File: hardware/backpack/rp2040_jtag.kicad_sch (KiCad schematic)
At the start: 27 parts, among them U1 ZD25WQ16CSIGT(SOIC-8_208mils), U2 RP2040(QFN-56_7x7mm_P0.4mm), Y1 Crystal_GND24_Small

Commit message: start power
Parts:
- removed RP-BOOT1: YTS-A016-X, symbol OLIMEX_Buttons:T1107A(6x3,8x2,5MM)
- added SW2: ~, cynthion:SW_Tactile_SPST_Angled_TC-1109DE-B-F, symbol support_hardware:SW_SPST_shielded
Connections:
- net GND: now also SW2.1
- net ~{BOOTSEL}: now also SW2.2
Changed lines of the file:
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@@
-	)
-	(symbol
-		(lib_id "OLIMEX_Buttons:T1107A(6x3,8x2,5MM)")
-		(at 186.69 33.02 0)
-		(unit 1)
-		(exclude_from_sim no)
-		(in_bom yes)
-		(on_board yes)
-		(dnp no)
-		(property "Reference" "RP-BOOT1"
-			(at 194.818 28.448 0)
-			(effects
-				(font
-					(size 1.524 1.524)
-				)
-			)
-		)
-		(property "Value" "YTS-A016-X"
-			(at 186.69 35.56 0)
-			(effects
-				(font
-					(size 1.27 1.27)
-				)
-			)
-		)
-		(property "Footprint" ""
-			(at 186.6646 32.0548 0)
-			(effects
-				(font
-					(size 1.524 1.524)
-				)
-				(hide yes)
-			)
-		)
-		(property "Datasheet" ""
-			(at 186.6646 32.0548 0)
-			(effects
-				(font
-					(size 1.524 1.524)
-				)
-			)
-		)
-		(property "Description" ""
-			(at 186.69 33.02 0)
-			(effects
-				(font
-					(size 1.27 1.27)
-				)
-				(hide yes)
-			)
-		)
-		(property "lcsc#" "C2910673"
-			(at 186.69 33.02 0)
-			(effects
-				(font
-					(size 1.27 1.27)
-				)
-				(hide yes)
-			)
-		)
-		(pin "1"
-		)
-		(pin "2"
-		)
-		(instances
-			(project "backpack"
-				(path "/df6062c3-a570-4505-924c-c7fe32df3670/32fbecb8-cfc0-4e90-9d95-f47a131c8376"
-					(reference "RP-BOOT1")
-					(unit 1)
-				)
-			)
-		)
 	)
 	(symbol
@@
 					(unit 1)
 				)
+			)
+		)
+	)
+	(symbol
+		(lib_id "support_hardware:SW_SPST_shielded")
+		(at 186.69 33.02 180)
+		(unit 1)
+		(exclude_from_sim no)
+		(in_bom yes)
+		(on_board yes)
+		(dnp no)
+		(property "Reference" "SW2"
+			(at 186.69 25.908 0)
+			(effects
+				(font
+					(size 1.27 1.27)
+				)
+			)
+		)
+		(property "Value" "~"
+			(at 186.69 25.4 0)
+			(effects
+				(font
+					(size 1.27 1.27)
+				)
+			)
+		)
+		(property "Footprint" "cynthion:SW_Tactile_SPST_Angled_TC-1109DE-B-F"
+			(at 186.69 33.02 0)
+			(effects
+				(font
+					(size 1.27 1.27)
+				)
+				(hide yes)
+			)
+		)
+		(property "Datasheet" "~"
+			(at 186.69 33.02 0)
+			(effects
+				(font
+					(size 1.27 1.27)
+				)
+				(hide yes)
+			)
+		)
+		(property "Description" "SWITCH TACTILE SPST-NO 0.05A 12V"
+			(at 186.69 33.02 0)
+			(effects
+				(font
+					(size 1.27 1.27)
+				)
+				(hide yes)
+			)
+		)
+		(property "Manufacturer" "XKB"
+			(at 186.69 33.02 0)
+			(effects
+				(font
+					(size 1.27 1.27)
+				)
+				(hide yes)
+			)
+		)
+		(property "Part Number" "TC-1109DE-B-F"
+			(at 186.69 33.02 0)
+			(effects
+				(font
+					(size 1.27 1.27)
+				)
+				(hide yes)
+			)
+		)
+		(property "Substitution" "DEALON TC-1150DL-6.0H-160"
+			(at 186.69 33.02 0)
+			(effects
+				(font
+					(size 1.27 1.27)
+				)
+				(hide yes)
+			)
+		)
+		(property "lcsc#" "C692468"
+			(at 186.69 33.02 0)
+			(effects
+				(font
+					(size 1.27 1.27)
+				)
+				(hide yes)
+			)
+		)
+		(pin "1"
+		)
+		(pin "2"
+		)
+		(pin "3"
+		)
+		(instances
+			(project "backpack"
+				(path "/df6062c3-a570-4505-924c-c7fe32df3670/32fbecb8-cfc0-4e90-9d95-f47a131c8376"
+					(reference "SW2")
+					(unit 1)
+				)

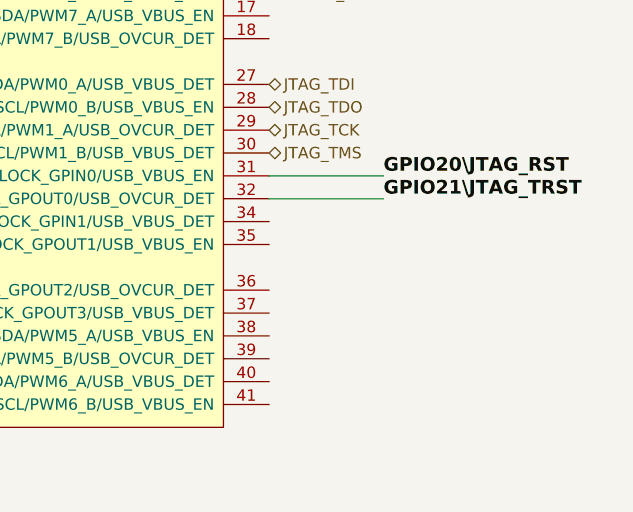
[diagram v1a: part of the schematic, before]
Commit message: parts and capture done sans most needing future pinswaps
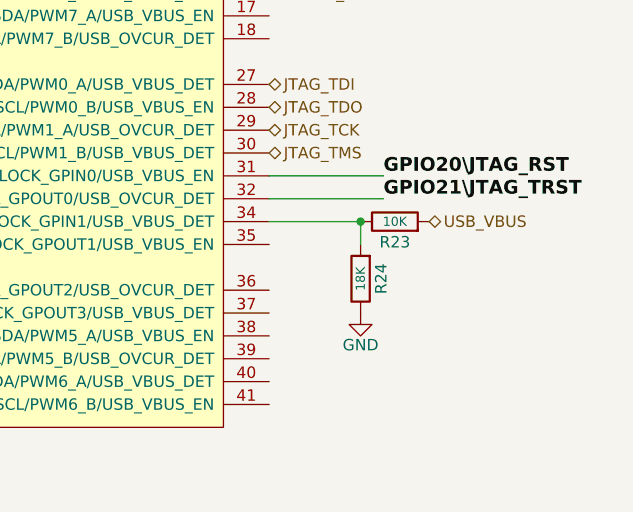
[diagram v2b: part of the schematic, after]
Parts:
- added R23: 10K, Resistor_SMD:R_0402_1005Metric, symbol OLIMEX_RCL:R
- added R24: 18K, Resistor_SMD:R_0402_1005Metric, symbol OLIMEX_RCL:R
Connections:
- net GND: now also R24.1
- net at U2.34 (GPIO22/SPI0_SCK/UART1_CTS/I2C1_SDA/PWM3_A/CLOCK_GPIN1/USB_VBUS_DET): now also R23.1, R24.2
- new net USB_VBUS: R23.2

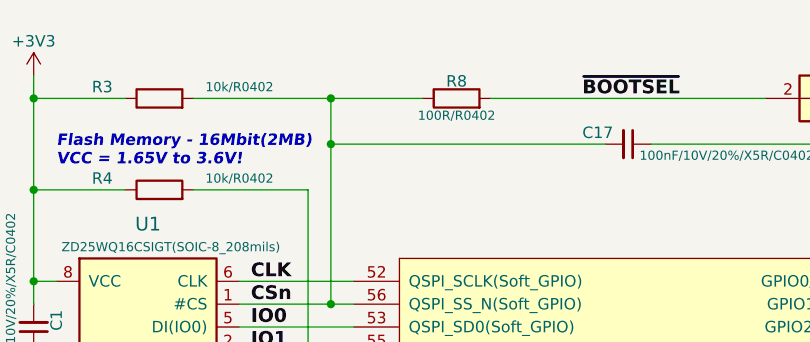
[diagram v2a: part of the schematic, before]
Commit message: place 2 leds, route 2nd button to both FPGA and RP2040
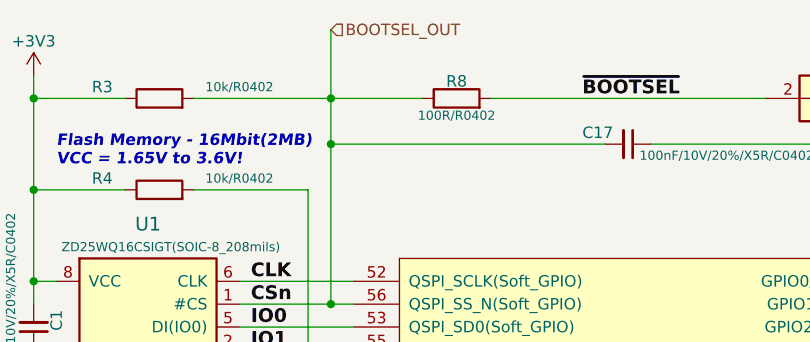
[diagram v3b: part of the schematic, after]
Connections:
- net CSn renamed BOOTSEL_OUT
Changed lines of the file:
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@@
+	(wire
+		(pts
+			(xy 130.81 25.4) (xy 130.81 33.02)
+		)
+		(stroke
+			(width 0)
+			(type default)
+		)
+	)
 	(wire
 		(pts
@@
 		)
 	)
+	(hierarchical_label "BOOTSEL_OUT"
+		(shape input)
+		(at 130.81 25.4 0)
+		(fields_autoplaced yes)
+		(effects
+			(font
+				(size 1.27 1.27)
+			)
+			(justify left)
+		)
+	)

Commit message: fix footprint errors and pin assignments on ffc
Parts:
- C11, C12: lcsc# (none) -> C12530
- C15, C16: lcsc# (none) -> C1549
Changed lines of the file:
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@@
+			)
+		)
+		(property "lcsc#" "C1549"
+			(at 102.87 132.08 0)
+			(effects
+				(font
+					(size 1.27 1.27)
+				)
+				(hide yes)
 			)
 		)
@@
 			)
 		)
+		(property "lcsc#" "C12530 "
+			(at 102.87 109.22 0)
+			(effects
+				(font
+					(size 1.27 1.27)
+				)
+				(hide yes)
+			)
+		)
 		(pin "1"
 		)
@@
 			)
 		)
+		(property "lcsc#" "C1549"
+			(at 102.87 137.16 0)
+			(effects
+				(font
+					(size 1.27 1.27)
+				)
+				(hide yes)
+			)
+		)
 		(pin "1"
 		)
@@
 			(at 102.87 114.3 0)
 			(effects
+				(font
+					(size 1.27 1.27)
+				)
+				(hide yes)
+			)
+		)
+		(property "lcsc#" "C12530 "
+			(at 102.87 114.3 0)
+			(effects

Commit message: updates before fab 04-04-24
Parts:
- C1, C10, C13, C14, C17, C2, C3, C4, C5, C6, C7, C8, C9: value 100nF/10V/20%/X5R/C0402 -> 0.1uF; lcsc# C129131 -> C307331
- R23: lcsc# C60490 -> C25744
- R24: lcsc# C60490 -> C138044
- R3, R4: value 10k/R0402 -> 10K; lcsc# C60490 -> C25744
- R5, R8: value 100R/R0402 -> 100R; lcsc# C106232 -> C25076
- R6, R7: value 27R/R0402 -> 27R
- SW2: value ~ -> SW_Tactile_SPST
- U1: footprint Package_SO:SOP-8_3.9x4.9mm_P1.27mm -> Package_SO:SOIC-8W_5.3x5.3mm_P1.27mm
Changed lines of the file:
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@@
 			)
 		)
-		(property "Value" "27R/R0402"
+		(property "Value" "27R"
 			(at 121.92 85.598 0)
 			(effects
@@
 			)
 		)
-		(property "Datasheet" ""
+		(property "Datasheet" "~"
 			(at 121.92 83.82 90)
 			(effects
@@
 			)
 		)
-		(property "Value" "100nF/10V/20%/X5R/C0402"
+		(property "Value" "0.1uF"
 			(at 104.14 87.63 90)
 			(effects
@@
 			)
 		)
-		(property "lcsc#" "C129131"
+		(property "lcsc#" " C307331"
 			(at 102.87 88.9 0)
 			(effects
@@
 			)
 		)
-		(property "Datasheet" ""
+		(property "Datasheet" "~"
 			(at 250.19 120.65 90)
 			(effects
@@
 			)
 		)
-		(property "lcsc#" "C60490"
+		(property "lcsc#" " C138044"
 			(at 250.19 120.65 0)
 			(effects
@@
 			)
 		)
-		(property "Value" "~"
+		(property "Value" "SW_Tactile_SPST"
 			(at 186.69 25.4 0)
 			(effects
@@
 			)
 		)
-		(property "lcsc#" "C60490"
+		(property "lcsc#" "C25744"
 			(at 254 114.3 0)
 			(effects
@@
 			)
 		)
-		(property "Value" "100nF/10V/20%/X5R/C0402"
+		(property "Value" "0.1uF"
 			(at 104.14 105.41 90)
 			(effects
@@
 			)
 		)
-		(property "lcsc#" "C129131"
+		(property "lcsc#" " C307331"
 			(at 102.87 106.68 0)
 			(effects
@@
 			)
 		)
-		(property "Value" "100R/R0402"
+		(property "Value" "100R"
 			(at 128.905 128.27 0)
 			(effects
@@
 			)
 		)
-		(property "Datasheet" ""
+		(property "Datasheet" "~"
 			(at 119.38 129.54 90)
 			(effects
@@
 			)
 		)
-		(property "lcsc#" "  C106232"
+		(property "lcsc#" "C25076"
 			(at 119.38 129.54 0)
 			(effects
@@
 			)
 		)
-		(property "Value" "100nF/10V/20%/X5R/C0402"
+		(property "Value" "0.1uF"
 			(at 104.14 100.33 90)
 			(effects
@@
 			)
 		)
-		(property "lcsc#" "C129131"
+		(property "lcsc#" " C307331"
 			(at 102.87 101.6 0)
 			(effects
@@
 			)
 		)
-		(property "Value" "100nF/10V/20%/X5R/C0402"
+		(property "Value" "0.1uF"
 			(at 104.14 120.65 90)
 			(effects
@@
 			)
 		)
-		(property "lcsc#" "C129131"
+		(property "lcsc#" " C307331"
 			(at 102.87 119.38 0)
 			(effects
@@
 			)
 		)
-		(property "Value" "100R/R0402"
+		(property "Value" "100R"
 			(at 144.78 34.925 0)
 			(effects
@@
 			)
 		)
-		(property "Datasheet" ""
+		(property "Datasheet" "~"
 			(at 144.78 33.02 90)
 			(effects
@@
 			)
 		)
-		(property "lcsc#" "  C106232"
+		(property "lcsc#" "C25076"
 			(at 144.78 33.02 0)
 			(effects
@@
 			)
 		)
-		(property "Datasheet" ""
+		(property "Datasheet" "~"
 			(at 102.87 132.08 0)
 			(effects
@@
 			)
 		)
-		(property "Value" "10k/R0402"
+		(property "Value" "10K"
 			(at 120.65 31.75 0)
 			(effects
@@
 			)
 		)
-		(property "lcsc#" "C60490"
+		(property "lcsc#" "C25744"
 			(at 111.76 33.02 0)
 			(effects
@@
 			)
 		)
-		(property "Footprint" "Package_SO:SOP-8_3.9x4.9mm_P1.27mm"
+		(property "Footprint" "Package_SO:SOIC-8W_5.3x5.3mm_P1.27mm"
 			(at 113.03 77.47 0)
 			(effects
@@
 			)
 		)
-		(property "Value" "100nF/10V/20%/X5R/C0402"
+		(property "Value" "0.1uF"
 			(at 104.14 97.79 90)
 			(effects
@@
 			)
 		)
-		(property "lcsc#" "C129131"
+		(property "lcsc#" " C307331"
 			(at 102.87 99.06 0)
 			(effects
@@
 			)
 		)
-		(property "Datasheet" ""
+		(property "Datasheet" "~"
 			(at 102.87 109.22 0)
 			(effects
@@
 			)
 		)
-		(property "Value" "27R/R0402"
+		(property "Value" "27R"
 			(at 121.92 79.375 0)
 			(effects
@@
 			)
 		)
-		(property "Datasheet" ""
+		(property "Datasheet" "~"
 			(at 121.92 81.28 90)
 			(effects
@@
 			)
 		)
-		(property "Value" "100nF/10V/20%/X5R/C0402"
+		(property "Value" "0.1uF"
 			(at 165.1 39.37 90)
 			(effects
@@
 			)
 		)
-		(property "lcsc#" "C129131"
+		(property "lcsc#" " C307331"
 			(at 163.83 38.1 0)
 			(effects
@@
 			)
 		)
-		(property "Value" "100nF/10V/20%/X5R/C0402"
+		(property "Value" "0.1uF"
 			(at 95.25 45.72 90)
 			(effects
@@
 			)
 		)
-		(property "lcsc#" "C129131"
+		(property "lcsc#" " C307331"
 			(at 97.79 58.42 0)
 			(effects
@@
 			)
 		)
-		(property "Value" "100nF/10V/20%/X5R/C0402"
+		(property "Value" "0.1uF"
 			(at 104.14 118.11 90)
 			(effects
@@
 			)
 		)
-		(property "lcsc#" "C129131"
+		(property "lcsc#" " C307331"
 			(at 102.87 116.84 0)
 			(effects
@@
 			)
 		)
-		(property "Value" "10k/R0402"
+		(property "Value" "10K"
 			(at 120.65 41.91 0)
 			(effects
@@
 			)
 		)
-		(property "lcsc#" "C60490"
+		(property "lcsc#" "C25744"
 			(at 111.76 43.18 0)
 			(effects
@@
 			)
 		)
-		(property "Datasheet" ""
+		(property "Datasheet" "~"
 			(at 102.87 137.16 0)
 			(effects
@@
 			)
 		)
-		(property "Value" "100nF/10V/20%/X5R/C0402"
+		(property "Value" "0.1uF"
 			(at 104.14 102.87 90)
 			(effects
@@
 			)
 		)
-		(property "lcsc#" "C129131"
+		(property "lcsc#" " C307331"
 			(at 102.87 104.14 0)
 			(effects
@@
 			)
 		)
-		(property "Value" "100nF/10V/20%/X5R/C0402"
+		(property "Value" "0.1uF"
 			(at 104.14 92.71 90)
 			(effects
@@
 			)
 		)
-		(property "lcsc#" "C129131"
+		(property "lcsc#" " C307331"
 			(at 102.87 93.98 0)
 			(effects
@@
 			)
 		)
-		(property "Datasheet" ""
+		(property "Datasheet" "~"
 			(at 102.87 114.3 0)
 			(effects
@@
 			)
 		)
-		(property "Value" "100nF/10V/20%/X5R/C0402"
+		(property "Value" "0.1uF"
 			(at 104.14 74.93 90)
 			(effects
@@
 			)
 		)
-		(property "lcsc#" "C129131"
+		(property "lcsc#" " C307331"
 			(at 102.87 76.2 0)
 			(effects
@@
 			)
 		)
-		(property "Value" "100nF/10V/20%/X5R/C0402"
+		(property "Value" "0.1uF"
 			(at 104.14 90.17 90)
 			(effects
@@
 			)
 		)
-		(property "lcsc#" "C129131"
+		(property "lcsc#" " C307331"
 			(at 102.87 91.44 0)
 			(effects
@@
 			)
 		)
-		(property "Value" "100nF/10V/20%/X5R/C0402"
+		(property "Value" "0.1uF"
 			(at 104.14 95.25 90)
 			(effects
@@
 			)
 		)
-		(property "lcsc#" "C129131"
+		(property "lcsc#" " C307331"
 			(at 102.87 96.52 0)
 			(effects
